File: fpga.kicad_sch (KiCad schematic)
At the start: 0 parts

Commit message: stuff
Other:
- sheet FPGA pg.1 ports: added DI; removed none
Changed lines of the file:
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@@
 	(bus
 		(pts
-			(xy 99.06 34.29) (xy 99.06 76.2)
+			(xy 91.44 76.2) (xy 116.84 76.2)
 		)
 		(stroke
@@
 	(bus
 		(pts
-			(xy 91.44 76.2) (xy 99.06 76.2)
+			(xy 91.44 78.74) (xy 116.84 78.74)
 		)
 		(stroke
@@
 			)
 			(justify left bottom)
+		)
+	)
+	(hierarchical_label "DI"
+		(shape input)
+		(at 116.84 78.74 0)
+		(fields_autoplaced yes)
+		(effects
+			(font
+				(size 1.27 1.27)
+			)
+			(justify left)
+		)
+	)
+	(hierarchical_label "DO"
+		(shape output)
+		(at 116.84 76.2 0)
+		(fields_autoplaced yes)
+		(effects
+			(font
+				(size 1.27 1.27)
+			)
+			(justify left)
 		)
 	)
@@
 			)
 		)
+		(pin "DI" output
+			(at 91.44 78.74 0)
+			(effects
+				(font
+					(size 1.27 1.27)
+				)
+				(justify right)
+			)
+		)
 		(instances
 			(project "logix-core"
@@
 	)
 	(sheet
-		(at 176.53 64.77)
+		(at 312.42 166.37)
 		(size 33.655 40.005)
 		(fields_autoplaced yes)
@@
 		)
 		(property "Sheetname" "FPGA pg.3"
-			(at 176.53 64.0584 0)
+			(at 312.42 165.6584 0)
 			(effects
 				(font
@@
 		)
 		(property "Sheetfile" "fpga-pg3.kicad_sch"
-			(at 176.53 105.3596 0)
+			(at 312.42 206.9596 0)
 			(effects
 				(font
@@
 	)
 	(sheet
-		(at 125.73 64.77)
+		(at 262.89 113.03)
 		(size 34.925 40.005)
 		(fields_autoplaced yes)
@@
 		)
 		(property "Sheetname" "FPGA pg.2"
-			(at 125.73 64.0584 0)
+			(at 262.89 112.3184 0)
 			(effects
 				(font
@@
 		)
 		(property "Sheetfile" "fpga-pg2.kicad_sch"
-			(at 125.73 105.3596 0)
-			(effects
-				(font
+			(at 262.89 153.6196 0)
+			(effects
+				(font

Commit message: working on ddr3
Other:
- sheet FPGA pg.2 ports: added DDR3_ADDR, DDR3_BLOCK_ADDR, DDR3_CAS#, DDR3_CLK+, DDR3_CLK-, DDR3_CLK_EN, DDR3_CS#, DDR3_DQ, DDR3_LDM, DDR3_LDQS+, DDR3_LDQS-, DDR3_ODT, DDR3_RAS#, DDR3_RESET#, DDR3_UDM, DDR3_UDQS+, DDR3_UDQS-, DDR3_WE#; removed none

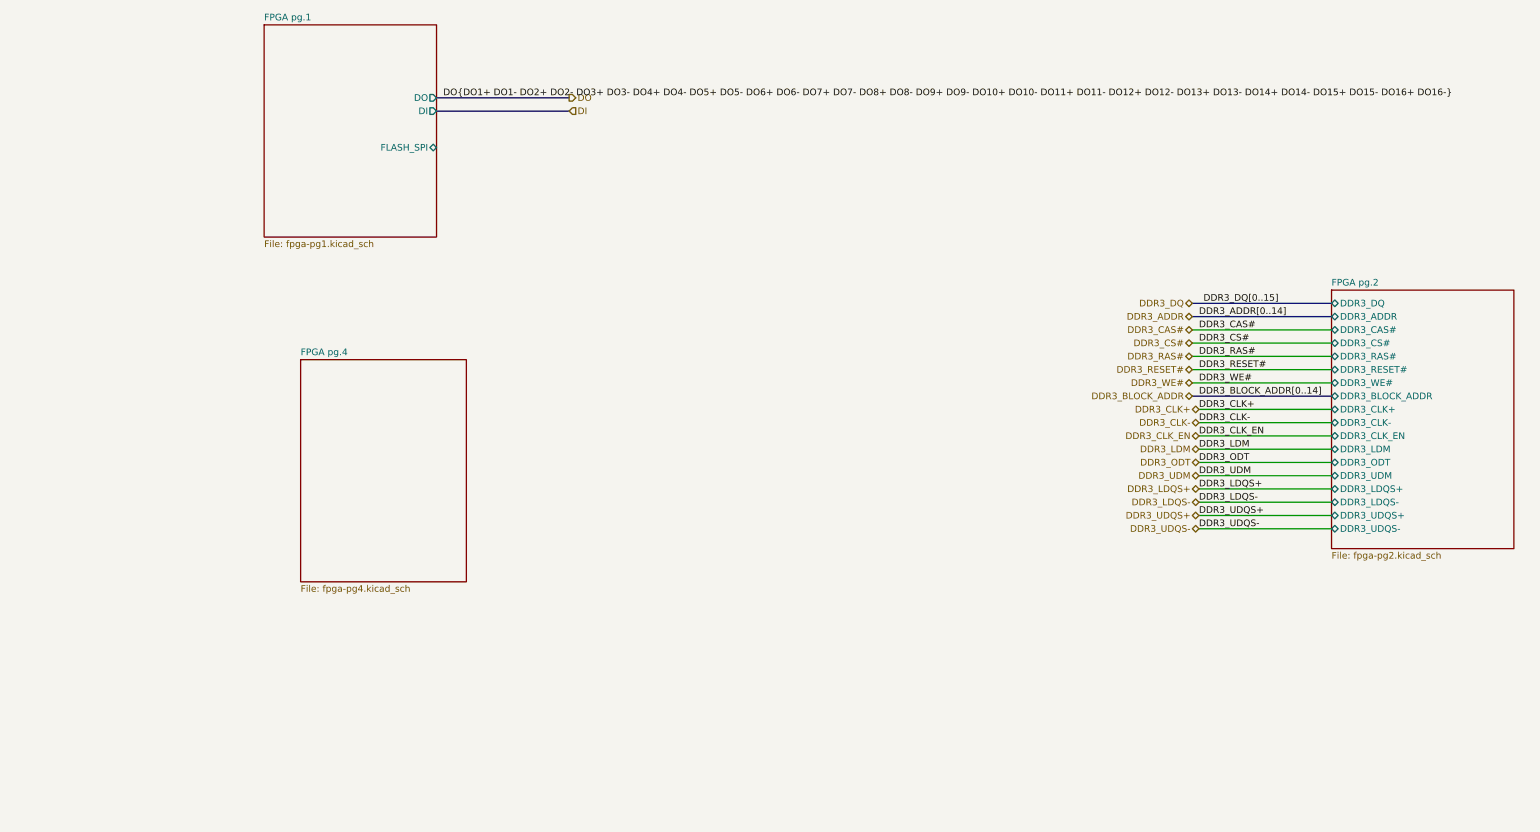
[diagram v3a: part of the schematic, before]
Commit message: changed ddr3 pinning according to hard-ip in vivado
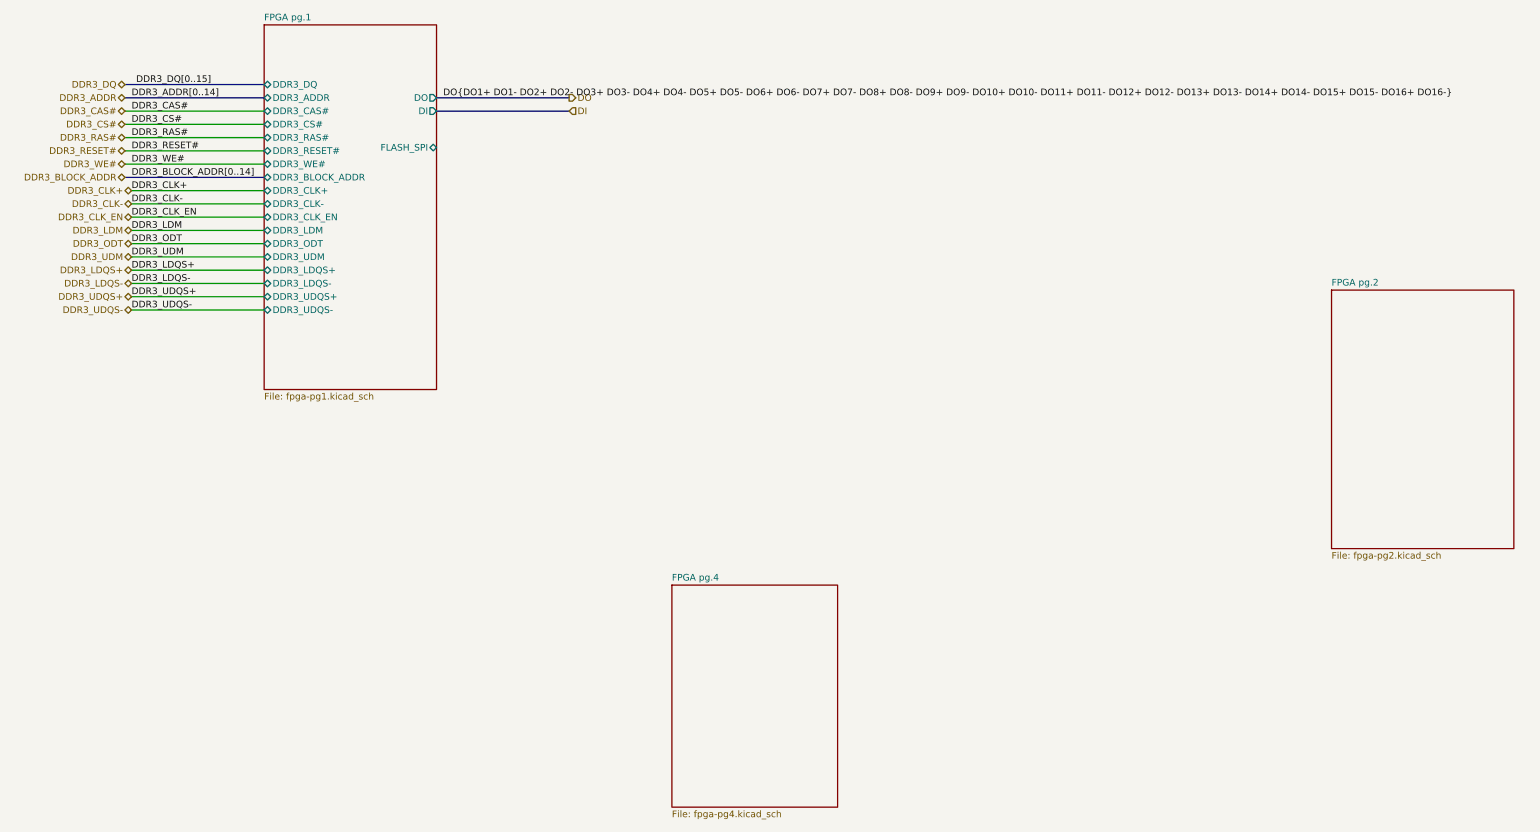
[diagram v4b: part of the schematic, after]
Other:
- sheet FPGA pg.1 ports: added DDR3_ADDR, DDR3_BLOCK_ADDR, DDR3_CAS#, DDR3_CLK+, DDR3_CLK-, DDR3_CLK_EN, DDR3_CS#, DDR3_DQ, DDR3_LDM, DDR3_LDQS+, DDR3_LDQS-, DDR3_ODT, DDR3_RAS#, DDR3_RESET#, DDR3_UDM, DDR3_UDQS+, DDR3_UDQS-, DDR3_WE#; removed none
- sheet FPGA pg.2 ports: added none; removed DDR3_ADDR, DDR3_BLOCK_ADDR, DDR3_CAS#, DDR3_CLK+, DDR3_CLK-, DDR3_CLK_EN, DDR3_CS#, DDR3_DQ, DDR3_LDM, DDR3_LDQS+, DDR3_LDQS-, DDR3_ODT, DDR3_RAS#, DDR3_RESET#, DDR3_UDM, DDR3_UDQS+, DDR3_UDQS-, DDR3_WE#

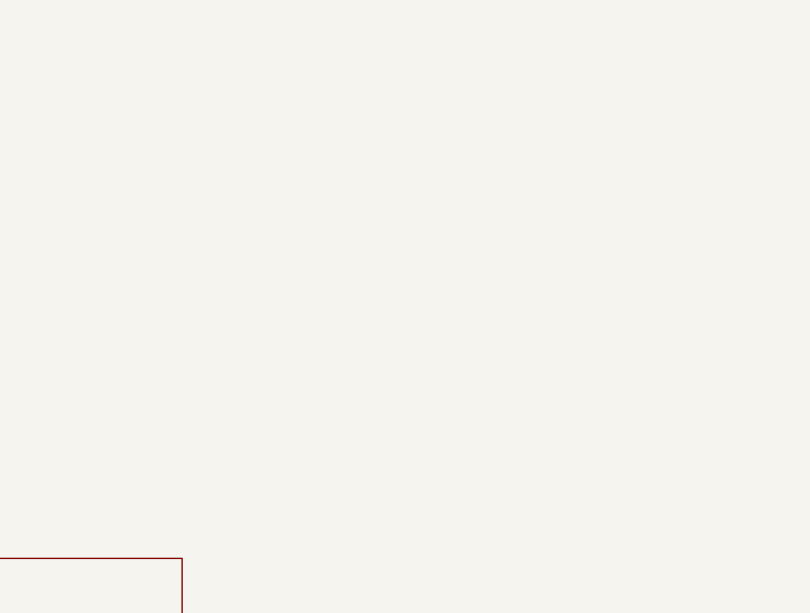
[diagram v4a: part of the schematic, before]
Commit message: started changing package, added correct decoupling
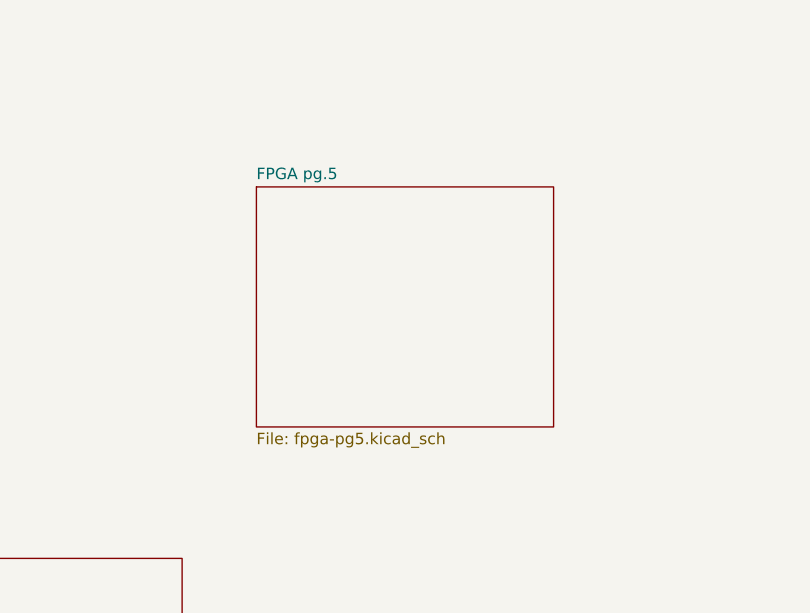
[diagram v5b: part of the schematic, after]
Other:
- added sheet FPGA pg.5 (fpga-pg5.kicad_sch)
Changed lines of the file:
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@@
+	)
+	(sheet
+		(at 176.53 128.27)
+		(size 33.02 26.67)
+		(exclude_from_sim no)
+		(in_bom yes)
+		(on_board yes)
+		(dnp no)
+		(fields_autoplaced yes)
+		(stroke
+			(width 0.1524)
+			(type solid)
+		)
+		(fill
+			(color 0 0 0 0.0000)
+		)
+		(property "Sheetname" "FPGA pg.5"
+			(at 176.53 127.5584 0)
+			(effects
+				(font
+					(size 1.27 1.27)
+				)
+				(justify left bottom)
+			)
+		)
+		(property "Sheetfile" "fpga-pg5.kicad_sch"
+			(at 176.53 155.5246 0)
+			(effects
+				(font
+					(size 1.27 1.27)
+				)
+				(justify left top)
+			)
+		)
+		(instances
+			(project "logix-core"
+				(path "/cf3b7c5f-6ddc-4e3f-9529-0bcf5eec6f23/824409ff-e0aa-4944-ad80-228eadb659f9"
+					(page "14")
+				)
+			)
+		)
 	)
 	(sheet

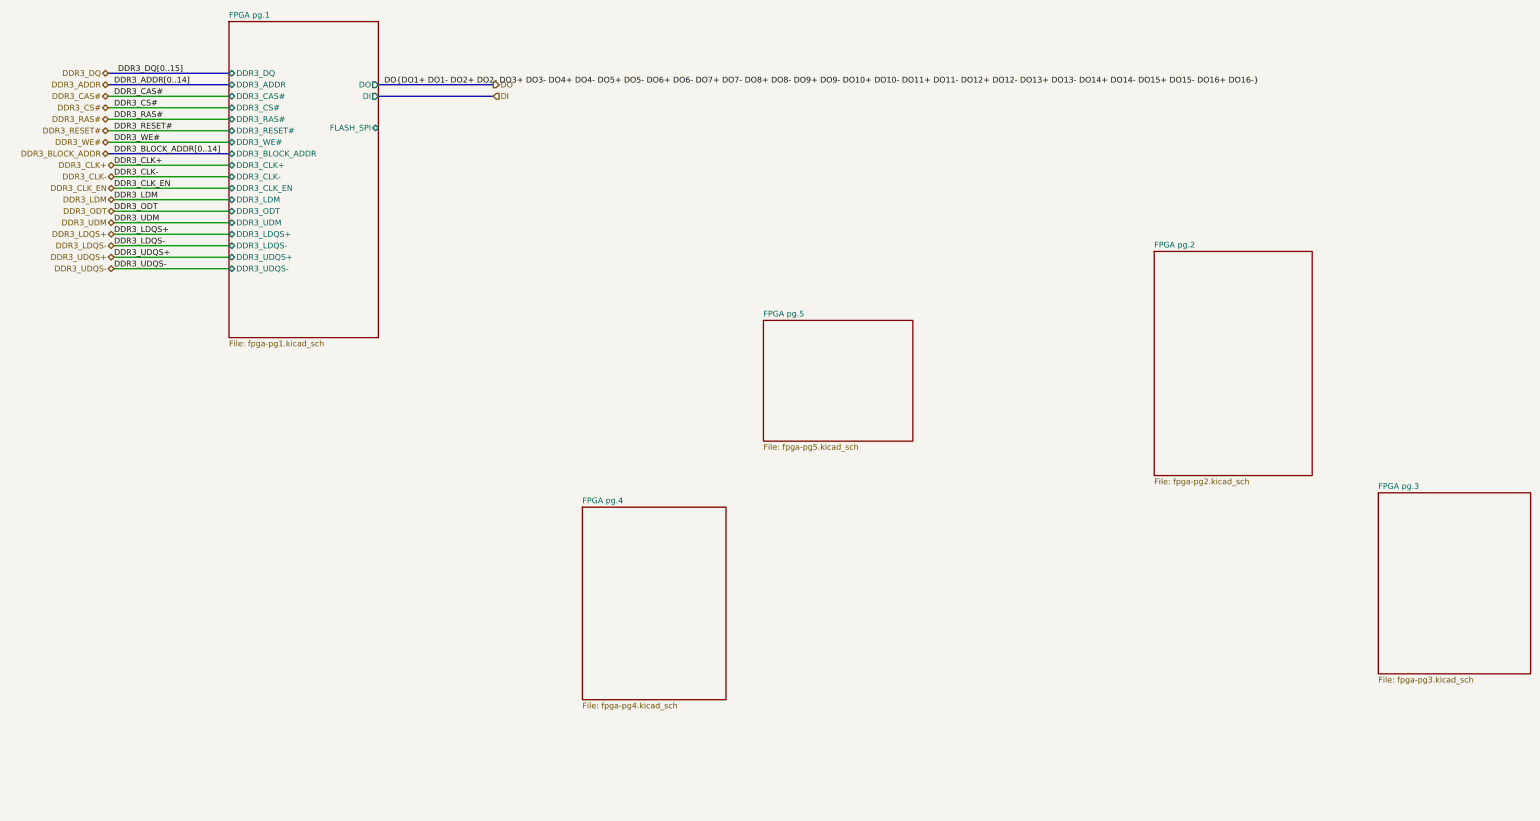
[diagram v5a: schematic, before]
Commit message: connected almost all ddr3 pins, started placing decoupling caps
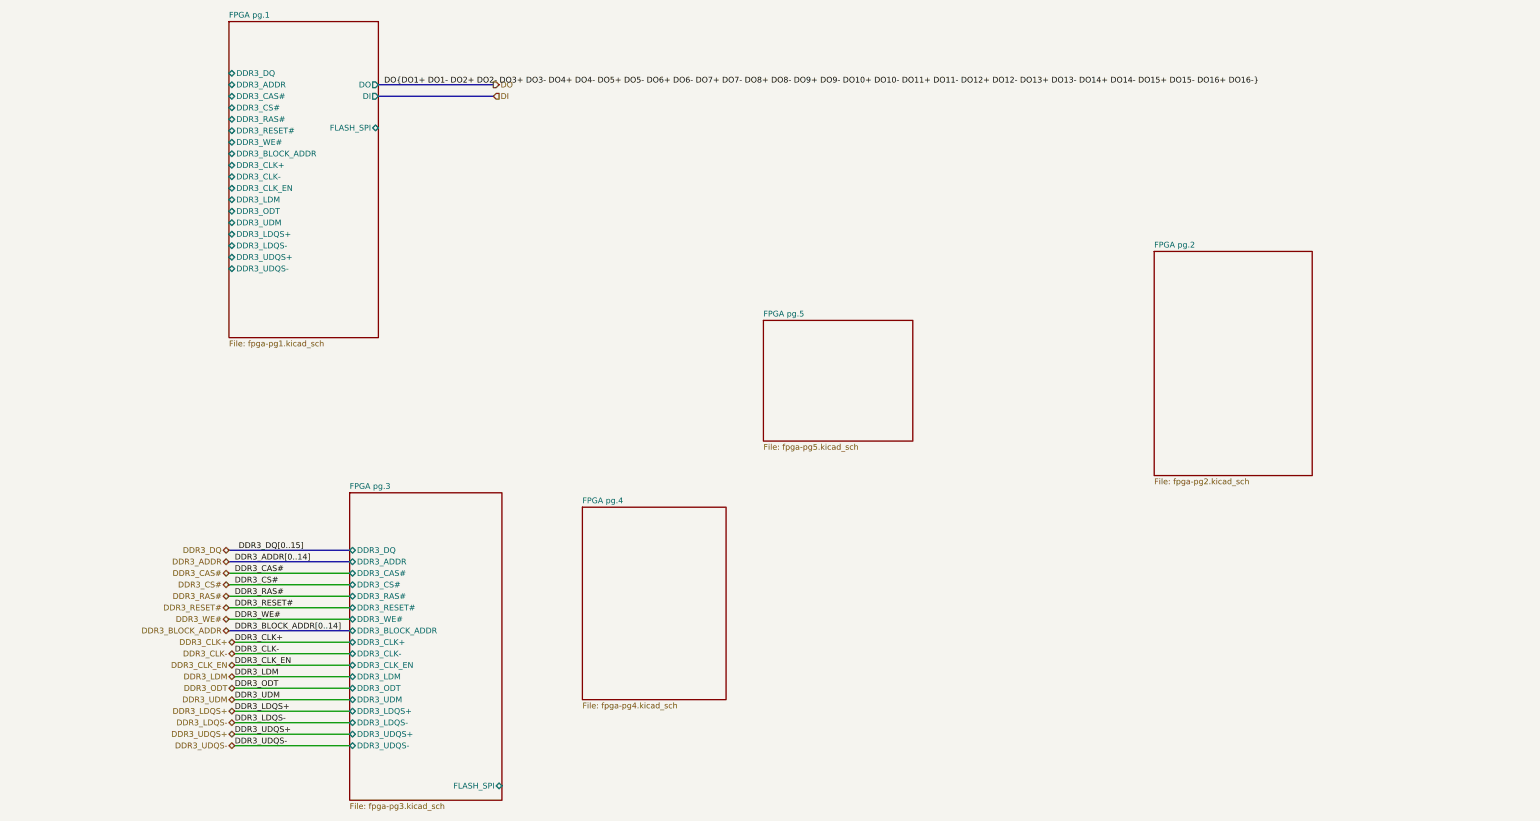
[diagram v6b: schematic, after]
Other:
- sheet FPGA pg.3 ports: added DDR3_ADDR, DDR3_BLOCK_ADDR, DDR3_CAS#, DDR3_CLK+, DDR3_CLK-, DDR3_CLK_EN, DDR3_CS#, DDR3_DQ, DDR3_LDM, DDR3_LDQS+, DDR3_LDQS-, DDR3_ODT, DDR3_RAS#, DDR3_RESET#, DDR3_UDM, DDR3_UDQS+, DDR3_UDQS-, DDR3_WE#, FLASH_SPI; removed none

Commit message: added a lot of stuff
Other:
- sheet FPGA pg.1 ports: added 7SEG1_A, 7SEG1_C, 7SEG2_A, 7SEG2_C, 7SEG3_A, 7SEG3_C; removed DDR3_ADDR, DDR3_BLOCK_ADDR, DDR3_CAS#, DDR3_CLK+, DDR3_CLK-, DDR3_CLK_EN, DDR3_CS#, DDR3_DQ, DDR3_LDM, DDR3_LDQS+, DDR3_LDQS-, DDR3_ODT, DDR3_RAS#, DDR3_RESET#, DDR3_UDM, DDR3_UDQS+, DDR3_UDQS-, DDR3_WE#, DI, DO, FLASH_SPI

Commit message: more floorplanning
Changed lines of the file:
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@@
+		)
+	)
+	(bus
+		(pts
+			(xy 119.38 231.14) (xy 152.4 231.14)
+		)
+		(stroke
+			(width 0)
+			(type default)
 		)
 	)
@@
 		)
 	)
+	(label "FLASH_SPI{D0 D1 D2 D3 CS#}"
+		(at 119.38 231.14 0)
+		(effects
+			(font
+				(size 1.27 1.27)
+			)
+			(justify left bottom)
+		)
+	)
 	(label "BTN1#"
 		(at 95.25 91.44 0)
@@
 			)
 			(justify right)
+		)
+	)
+	(hierarchical_label "FLASH_SPI"
+		(shape bidirectional)
+		(at 152.4 231.14 0)
+		(effects
+			(font
+				(size 1.27 1.27)
+			)
+			(justify left)
 		)
 	)
@@
 	(sheet
 		(at 85.09 166.37)
-		(size 33.655 67.945)
+		(size 34.29 68.58)
 		(exclude_from_sim no)
 		(in_bom yes)
@@
 		)
 		(property "Sheetfile" "fpga-pg3.kicad_sch"
-			(at 85.09 234.8996 0)
+			(at 85.09 235.5346 0)
 			(effects
 				(font
@@
 		)
 		(pin "FLASH_SPI" bidirectional
-			(at 118.745 231.14 0)
-			(effects
-				(font
+			(at 119.38 231.14 0)
+			(effects
+				(font
